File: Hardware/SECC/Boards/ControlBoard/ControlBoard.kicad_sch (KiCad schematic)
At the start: 10 parts

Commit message: Update SECC
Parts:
- added J1: UJ2-B-HR-G-V, InverterCom:UJ2BHRGV, symbol InverterCom:UJ2-B-HR-G-V
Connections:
- net GND_A: now also J1.4 (GND), J1.MH1, J1.MH2
- new net Main Processor/USB_OTG_HS_DM: J1.2 (D-)
- new net Main Processor/USB_OTG_HS_DP: J1.3 (D+)
- no-connect marks 24 -> 2
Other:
- added sheet Control Pilot Driver (CPDriver.kicad_sch)
- sheet Main Processor ports: added AIN_CABLE_TEMP, CP_FEEDBACK, CURSENS_A_REF, CURSENS_A_SIG, CURSENS_B_REF, CURSENS_B_SIG, DEBUG_SWCLK, DEBUG_SWDIO, ETH_CRS_DV, ETH_MDC, ETH_MDIO, ETH_REF_CLK, ETH_RXD0, ETH_RXD1, ETH_TXD0, ETH_TXD1, ETH_TX_EN, FDCAN3_RX, FDCAN3_TX, MAIN_CONTACTOR_OUT, PRECHARGE_CONTACTOR_OUT, PUMP_PWM, PWM_HIGH, PWM_LOW, SPI1_MISO, SPI1_MOSI, SPI1_SCK, USB_OTG_HS_DM, USB_OTG_HS_DP, USB_OTG_HS_ID; removed CANBUS_12V_POWER_ENABLE, COPROCESSOR_BOOTSEL, COPROCESSOR_RESET, COPROCESSOR_SYNC, COPROCESSOR_TIMER_SYNC_OUT, COPROCESSOR_WAKEUP, DC_LINK_CURRENT_COMPARITOR_N, DC_LINK_CURRENT_SENSE, DC_LINK_CURRENT_SENSE_REF, DEBUG_JTCK-SWCLK, DEBUG_JTCK-SWDIO, DEBUG_NJTRST, DEBUG_SWO, FDCAN1_RX, FDCAN1_TX, GATE_DRIVER_POWER_ENABLE, GATE_DRIVE_PWR1_FEEDBACK, GATE_DRIVE_PWR2_FEEDBACK, HALL_U_ENCODER_SIN, HALL_V_ENCODER_COS, HALL_W, MOTOR_TEMP, MULTIDRIVE_FIBER_SYNC, MULTIDRIVE_FIBER_UART_RX, MULTIDRIVE_FIBER_UART_TX, ONBOARD_TEMP_SENSE_I2C_SCL, ONBOARD_TEMP_SENSE_I2C_SDA, PERIPHERAL_POWER_ENABLE, PHASE_CURRENT_COMPARITOR_N, PHASE_U_CURRENT_SENSE, PHASE_U_CURRENT_SENSE_REF, PHASE_U_HIGH, PHASE_U_LOW, PHASE_V_CURRENT_SENSE, PHASE_V_CURRENT_SENSE_REF, PHASE_V_HIGH, PHASE_V_LOW, PHASE_W_CURRENT_SENSE, PHASE_W_CURRENT_SENSE_REF, PHASE_W_HIGH, PHASE_W_LOW, POWERMON_ENABLE, POWERMON_SLEEP, TEMP_SENSE_1, TEMP_SENSE_2, TEMP_SENSE_3, THROTTLE_A, THROTTLE_B, USART3_RX, USART3_TX, USER_DIN_1, USER_DIN_2, USER_DIN_3, USER_DIN_4, USER_DIN_5, USER_DIN_6, USER_DIN_7, USER_DIN_8, USER_DOUT_1, USER_DOUT_2, USER_DOUT_3, USER_DOUT_4, VOLTAGE_MONITOR_I2C_SCL, VOLTAGE_MONITOR_I2C_SDA
- sheet Power ports: added none; removed +12V_CANBUS_A, +12V_IN, +12V_SWITCHED_A, +5V_A, CANBUS_12V_ENABLE_A, SIGNAL_12V_ENABLE_A
- moved on the sheet: S1, S2

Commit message: Update SECC Schematic
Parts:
- removed J1: UJ2-B-HR-G-V, InverterCom:UJ2BHRGV, symbol InverterCom:UJ2-B-HR-G-V
- added J1: TBP02R2W-381-08BE, TBP02R2W38108BE, symbol InverterCom:TBP02R2W-381-08BE
- added J2: TBP02R2W-381-06BE, TBP02R2W38106BE, symbol InverterCom:TBP02R2W-381-06BE
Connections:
- net +12V_A: now also J2.3, J2.6
- net GND_A: now also J1.2, J1.8, J2.1, J2.4
- new net +CONTACTOR_VBUS: J2.5
- new net +PWM_VBUS: J2.2
- new net CABLE_THERMISTOR: J1.3
- new net CP_PIN: J1.1
- new net MAIN_CONTACTOR_OUT: J1.7
- new net PE_PIN: J1.4
- new net PRECHARGE_CONTACTOR_OUT: J1.6
- new net PUMP_PWM_OUT: J1.5
- no-connect marks 2 -> 0
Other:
- added sheet CCS Greenphy Modem (CCSModem.kicad_sch)
- added sheet CableIO (CableIO.kicad_sch)
- sheet Main Processor ports: added SPI1_CS; removed BOOT_SEL, DEBUG_SWCLK, DEBUG_SWDIO, DEBUG_TRGIO, ETH_CRS_DV, ETH_MDC, ETH_MDIO, ETH_REF_CLK, ETH_RXD0, ETH_RXD1, ETH_TXD0, ETH_TXD1, ETH_TX_EN, NRST, USB_OTG_HS_DM, USB_OTG_HS_DP, USB_OTG_HS_ID
- note added: "Connector to ccs/j1772 cable and contactors"
- note added: "contactor/pwm driver power"

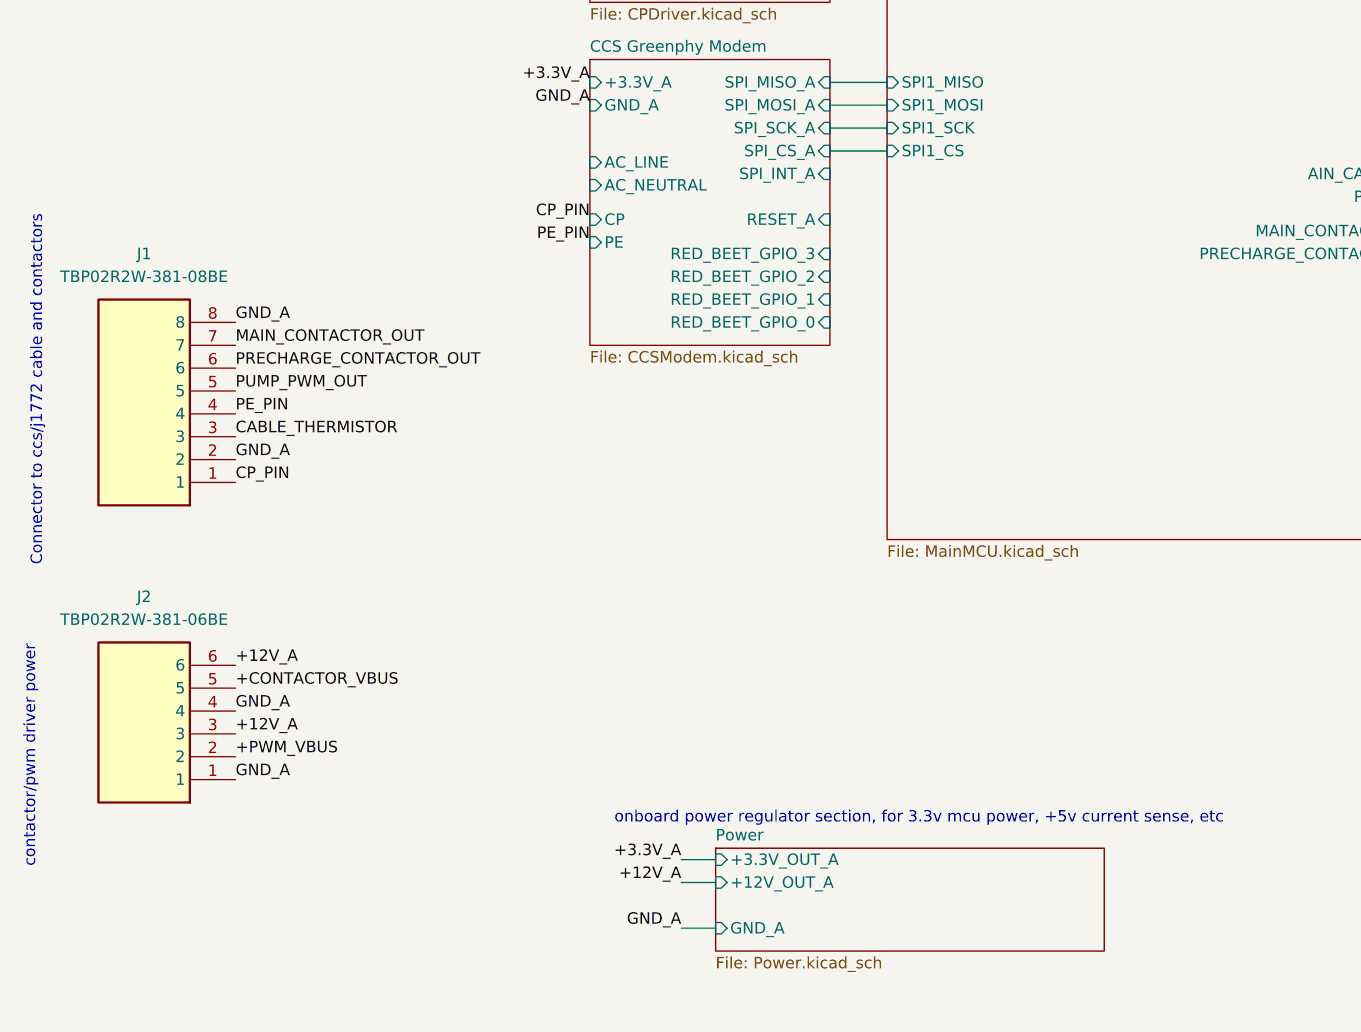
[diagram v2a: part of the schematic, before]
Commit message: Finish schematic
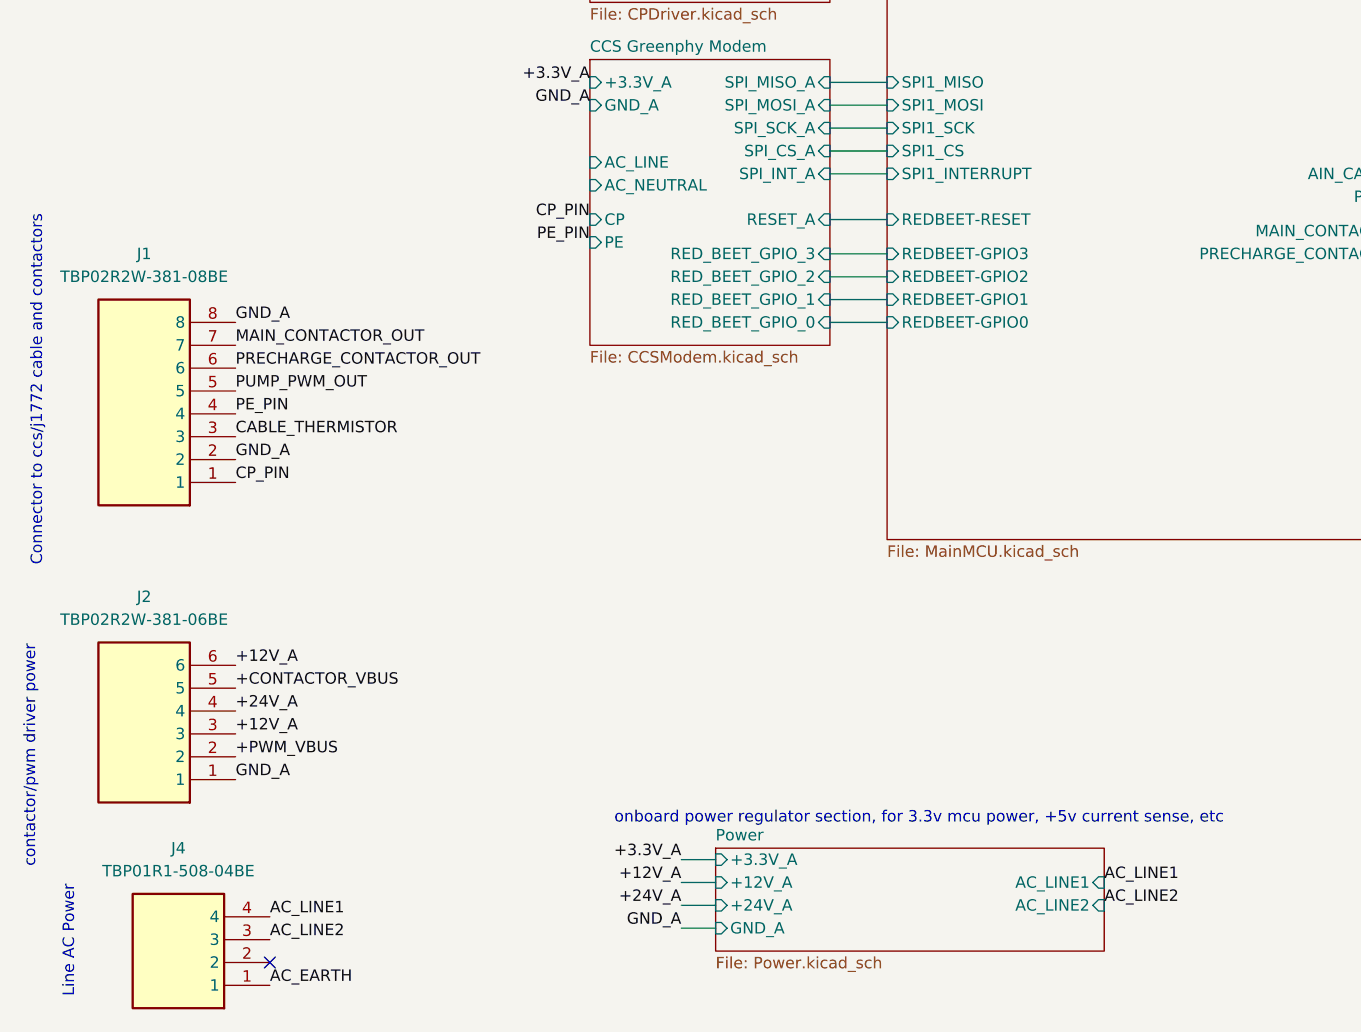
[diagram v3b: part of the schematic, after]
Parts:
- added J4: TBP01R1-508-04BE, TBP01R150804BE, symbol InverterCom:TBP01R1-508-04BE
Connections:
- net GND_A: no longer J2.4
- new net +24V_A: J2.4
- new net AC_EARTH: J4.1
- new net AC_LINE1: J4.4
- new net AC_LINE2: J4.3
- no-connect marks 0 -> 1
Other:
- sheet Main Processor ports: added REDBEET-GPIO0, REDBEET-GPIO1, REDBEET-GPIO2, REDBEET-GPIO3, REDBEET-RESET, SPI1_INTERRUPT; removed none
- sheet Power ports: added +12V_A, +24V_A, +3.3V_A, AC_LINE1, AC_LINE2; removed +12V_OUT_A, +3.3V_OUT_A
- note added: "Line AC Power"

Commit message: layout
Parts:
- removed J4: TBP01R1-508-04BE, TBP01R150804BE, symbol InverterCom:TBP01R1-508-04BE
- added J5, J7: TBP02R2W-381-06BE, InverterCom:TBP02R2W38106BE, symbol InverterCom:TBP02R2W-381-06BE
- added J8: TBP01R2-508-06BE, TBP01R250806BE, symbol InverterCom:TBP01R2-508-06BE
- added J9: TBP01R2-508-04BE, SHDR4W100P0X508_1X4_2192X850X1200P, symbol InverterCom:TBP01R2-508-04BE
- J1: footprint TBP02R2W38108BE -> InverterCom:TBP02R2W38108BE
- J2: footprint TBP02R2W38106BE -> InverterCom:TBP02R2W38106BE
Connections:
- net PE_PIN is gone; now on net GND_A: J1.4
- net +12V_A: now also J2.4; no longer J2.3, J2.6
- net +24V_A: now also J2.6; no longer J2.4
- net AC_EARTH: now also J9.1
- net AC_LINE1: now also J9.4
- net AC_LINE2: now also J9.3
- net CAN1_+5V: now also J7.4
- net CAN1_GND: now also J7.3
- net CAN1_HIGH: now also J7.2
- net CAN1_JUMPER_A: now also J7.5
- net CAN1_JUMPER_B: now also J7.6
- net CAN1_LOW: now also J7.1
- net CAN2_+5V: now also J5.4
- net CAN2_GND: now also J5.3
- net CAN2_HIGH: now also J5.2
- net CAN2_JUMPER_A: now also J5.5
- net CAN2_JUMPER_B: now also J5.6
- net CAN2_LOW: now also J5.1
- net GND_A: now also J2.3
- net VS_DC_LINK_Y: now also J8.1
- net VS_GND_Y: now also J8.5
- net VS_PH_U_Y: now also J8.2
- net VS_PH_V_Y: now also J8.3
- net VS_PH_W_Y: now also J8.4
- no-connect marks 1 -> 2
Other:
- note added: "our logic is tied to pe"

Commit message: esp32 stuff
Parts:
- removed H6, H7, H8: 971350581, InverterCom:971350581, symbol Mechanical:MountingHole
- removed S1, S2: TS40-66-50-R-260-SMT-TR, InverterCom:TS406650R260SMTTR, symbol InverterCom:TS40-66-50-R-260-SMT-TR
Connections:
- net AC_EARTH is gone; now on net GND_A: J9.1
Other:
- added sheet ESP32 CoProcessor (ESP32_COPROC.kicad_sch)
- note removed: "bootsel switch, push for bootloader"
- note removed: "reset switch, push to reset"

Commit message: esp32 progress
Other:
- sheet ESP32 CoProcessor ports: added ESP_BOOT, ESP_EN, ESP_SPI_CS, ESP_SPI_MISO, ESP_SPI_MOSI, ESP_SPI_SCK, ESP_UART_RX, ESP_UART_TX, ESP_USB_DM, ESP_USB_DP, GND, VCC_3.3V; removed none
